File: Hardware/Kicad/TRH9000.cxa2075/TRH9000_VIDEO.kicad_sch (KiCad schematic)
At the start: 30 parts, among them J1 S-Video, J2 RGB, Q1 BC817, U6 CXA2075M

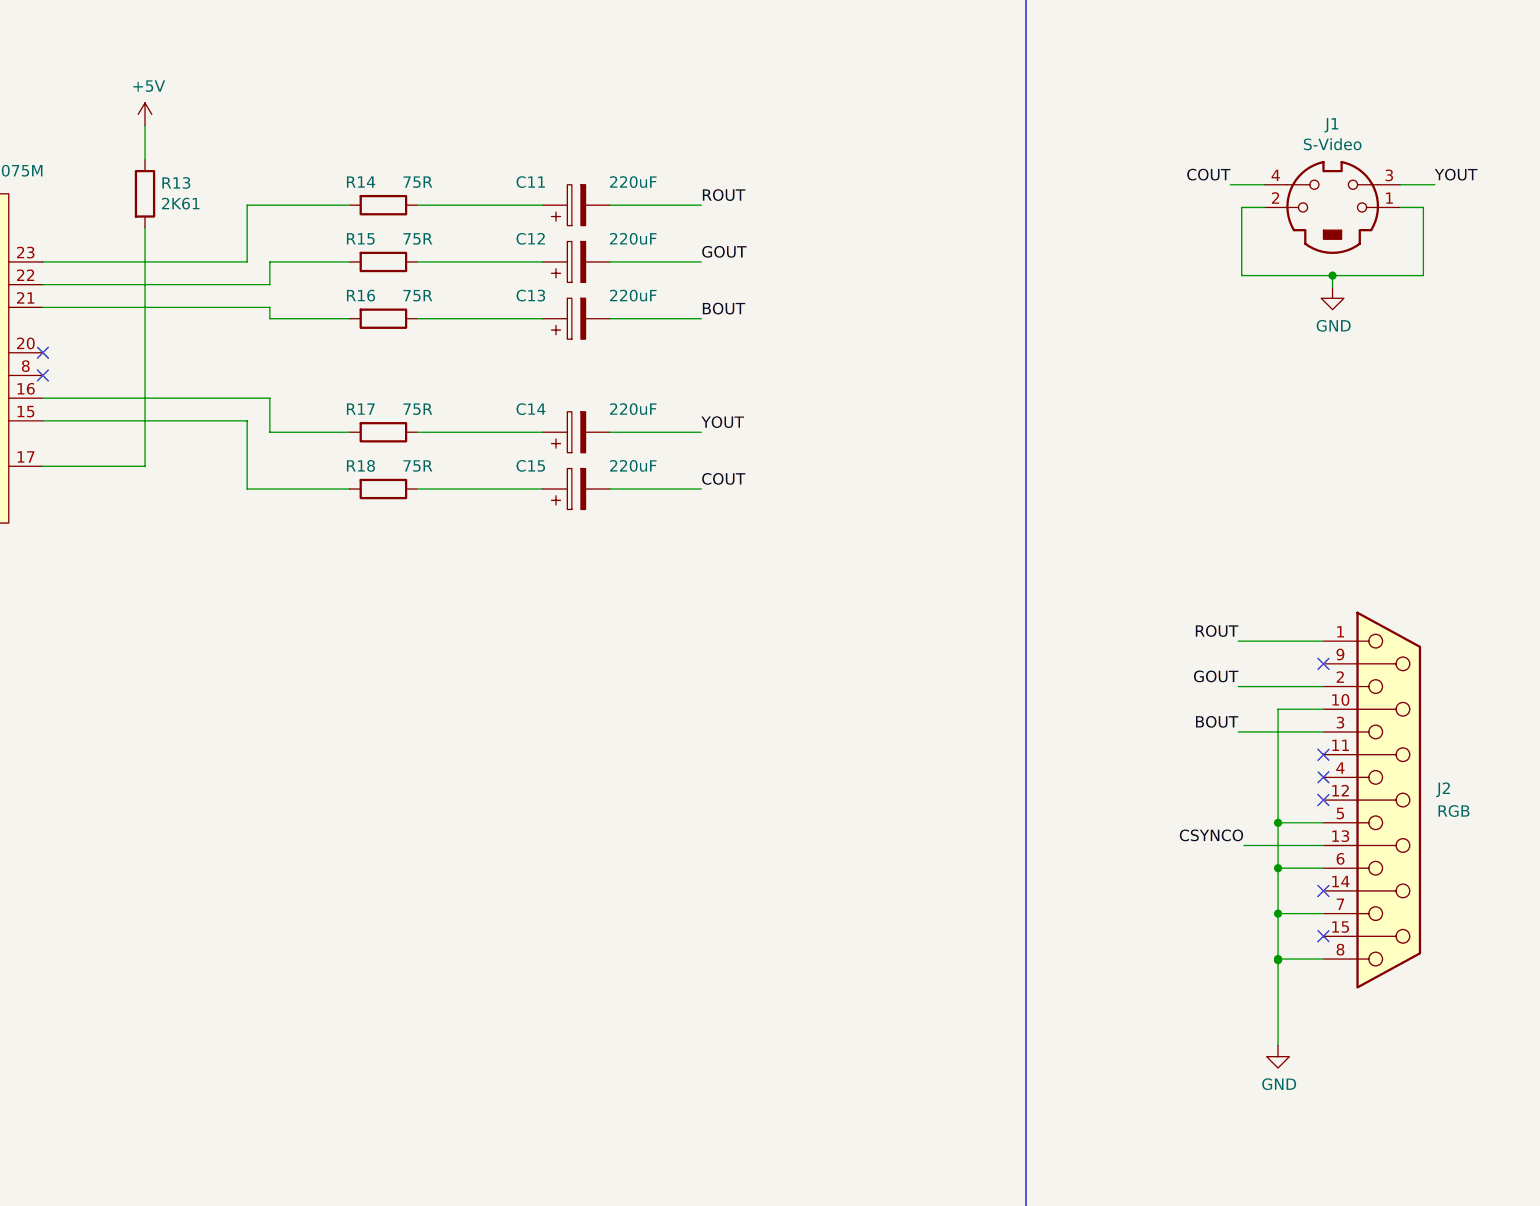
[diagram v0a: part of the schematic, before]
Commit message: small fix on the YTRAP to use internal for NTSC.
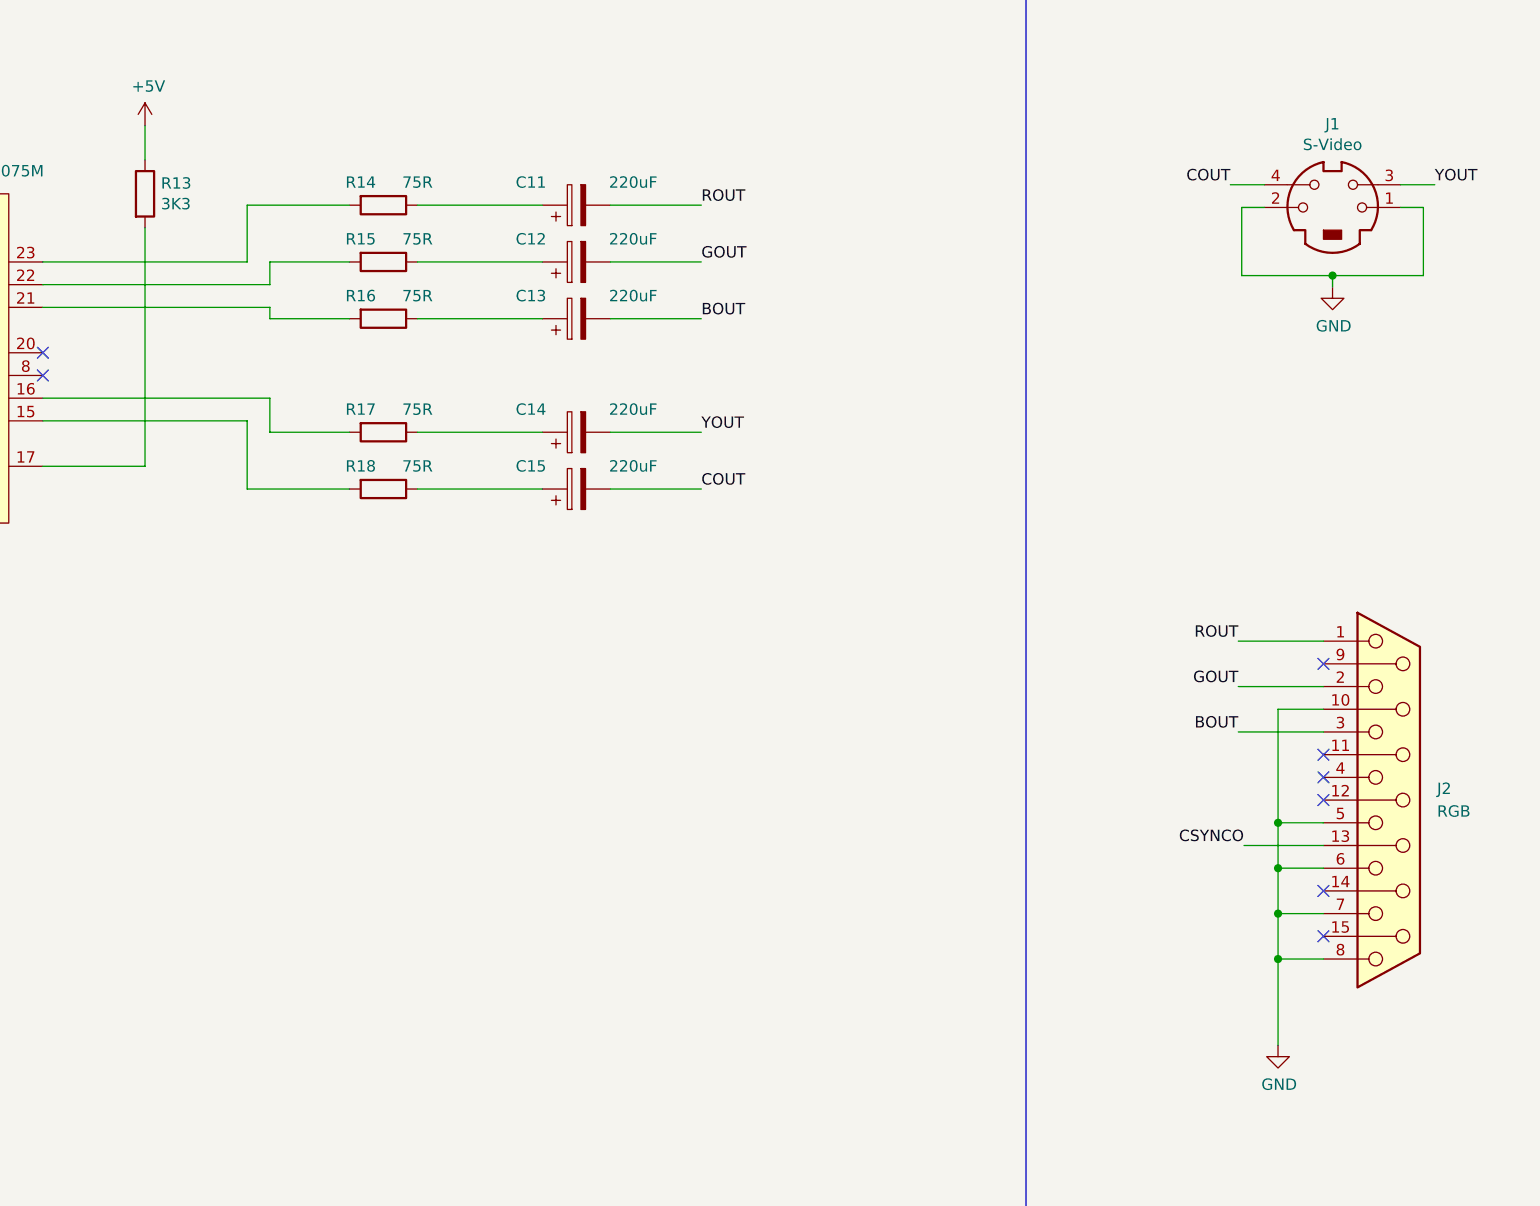
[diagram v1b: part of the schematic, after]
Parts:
- R13: value 2K61 -> 3K3

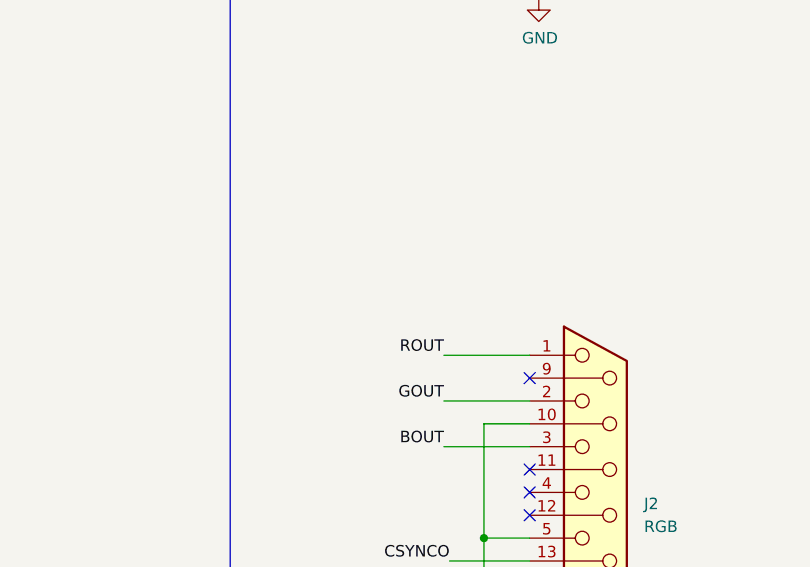
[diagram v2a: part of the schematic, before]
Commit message: Jumper to provide 5V to SCART cables
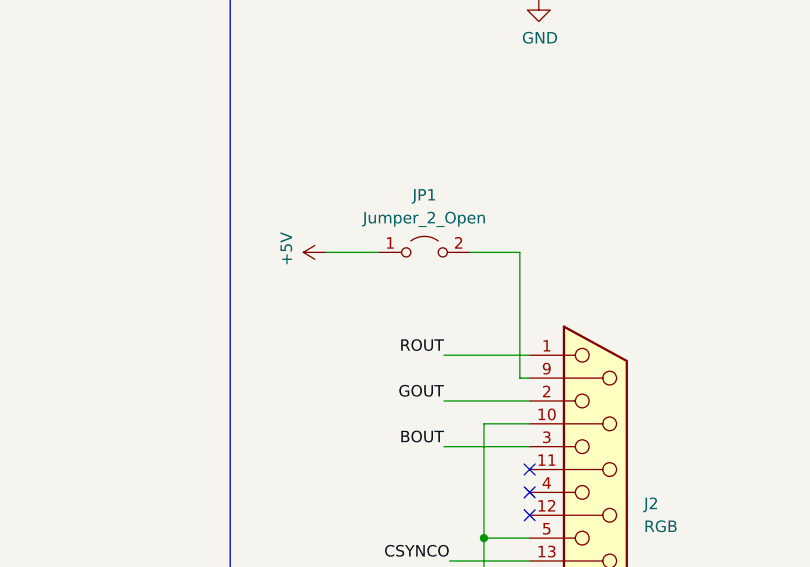
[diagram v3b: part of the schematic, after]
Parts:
- added JP1: Jumper_2_Open, Jumper:SolderJumper-2_P1.3mm_Open_Pad1.0x1.5mm, symbol Jumper:Jumper_2_Open
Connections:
- net +5V: now also JP1.1 (A)
- net at J2.9 (P9): now also JP1.2 (B)
- no-connect marks 8 -> 7
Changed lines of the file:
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@@
   (no_connect (at 165.608 113.284))
   (no_connect (at 308.864 170.942))
-  (no_connect (at 308.864 145.542))
   (no_connect (at 308.864 158.242))
   (no_connect (at 165.608 110.744))
@@
     (stroke (width 0) (type default))
   )
+  (wire (pts (xy 307.7718 145.542) (xy 307.7718 131.572))
+    (stroke (width 0) (type default))
+  )
   (wire (pts (xy 152.908 80.264) (xy 152.908 81.534))
     (stroke (width 0) (type default))
@@
     (stroke (width 0) (type default))
   )
+  (wire (pts (xy 302.26 131.572) (xy 307.7718 131.572))
+    (stroke (width 0) (type default))
+  )
   (wire (pts (xy 100.33 200.406) (xy 112.014 200.406))
     (stroke (width 0) (type default))
@@
     (stroke (width 0) (type default))
   )
+  (wire (pts (xy 308.864 145.542) (xy 307.7718 145.542))
+    (stroke (width 0) (type default))
+  )
   (wire (pts (xy 80.518 110.744) (xy 80.518 113.284))
     (stroke (width 0) (type default))
@@
   )
   (wire (pts (xy 165.608 103.124) (xy 191.008 103.124))
+    (stroke (width 0) (type default))
+  )
+  (wire (pts (xy 286.258 131.572) (xy 292.1 131.572))
     (stroke (width 0) (type default))
   )
@@
     )
   )
+  (symbol (lib_id "power:+5V") (at 286.258 131.572 90) (unit 1)
+    (in_bom yes) (on_board yes) (dnp no)
+    (property "Reference" "#PWR047" (at 290.068 131.572 0)
+      (effects (font (size 1.27 1.27)) hide)
+    )
+    (property "Value" "+5V" (at 281.8638 131.191 0)
+      (effects (font (size 1.27 1.27)))
+    )
+    (property "Footprint" "" (at 286.258 131.572 0)
+      (effects (font (size 1.27 1.27)) hide)
+    )
+    (property "Datasheet" "" (at 286.258 131.572 0)
+      (effects (font (size 1.27 1.27)) hide)
+    )
+    (pin "1")
+    (instances
+      (project "TRH9000"
+        (path "/1a0ec755-0979-4213-9180-0cd879831c1c/d9ed34ef-ff83-4a70-a9f7-db0f42d1292e"
+          (reference "#PWR047") (unit 1)
+        )
+      )
+    )
+  )
   (symbol (lib_id "Device:C") (at 80.518 117.094 0) (unit 1)
     (in_bom yes) (on_board yes) (dnp no)
@@
         )
       )
+    )
+  )
+  (symbol (lib_id "Jumper:Jumper_2_Open") (at 297.18 131.572 0) (unit 1)
+    (in_bom yes) (on_board yes) (dnp no) (fields_autoplaced)
+    (property "Reference" "JP1" (at 297.18 125.222 0)
+      (effects (font (size 1.27 1.27)))
+    )
+    (property "Value" "Jumper_2_Open" (at 297.18 127.762 0)
+      (effects (font (size 1.27 1.27)))
+    )
+    (property "Footprint" "Jumper:SolderJumper-2_P1.3mm_Open_Pad1.0x1.5mm" (at 297.18 131.572 0)
+      (effects (font (size 1.27 1.27)) hide)
+    )
+    (property "Datasheet" "~" (at 297.18 131.572 0)
+      (effects (font (size 1.27 1.27)) hide)
+    )
+    (pin "1")
+    (pin "2")
+    (instances
+      (project "TRH9000"
+        (path "/1a0ec755-0979-4213-9180-0cd879831c1c/d9ed34ef-ff83-4a70-a9f7-db0f42d1292e"
+          (reference "JP1") (unit 1)
+        )
+      )

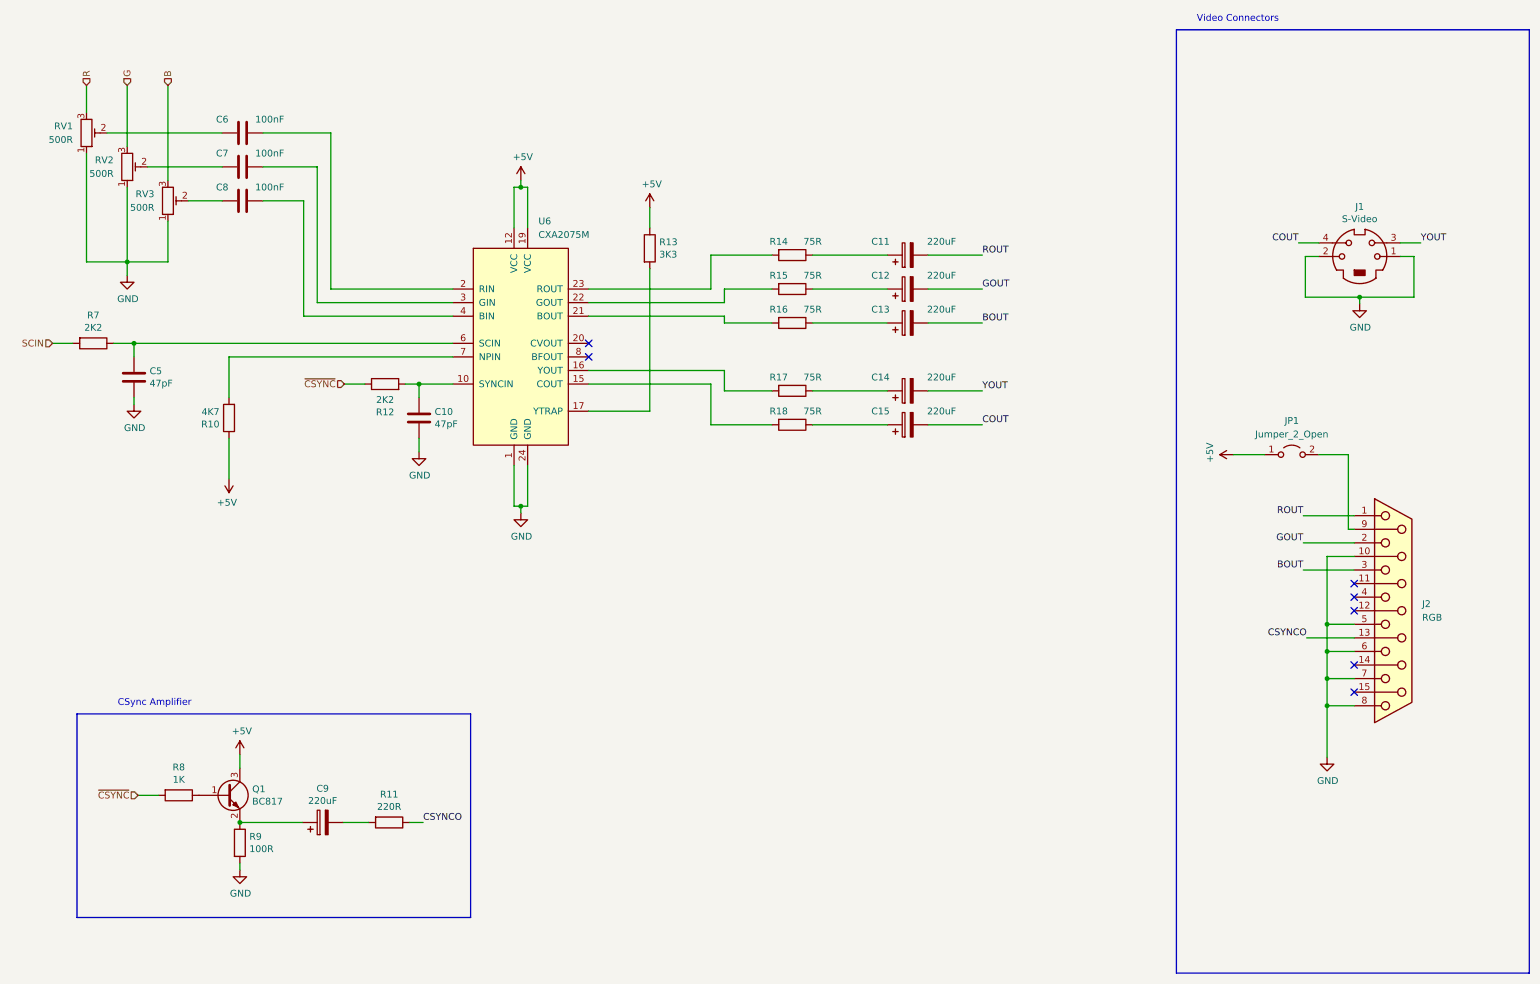
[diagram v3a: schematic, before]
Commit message: Exposing composite, footprint and silk corrections
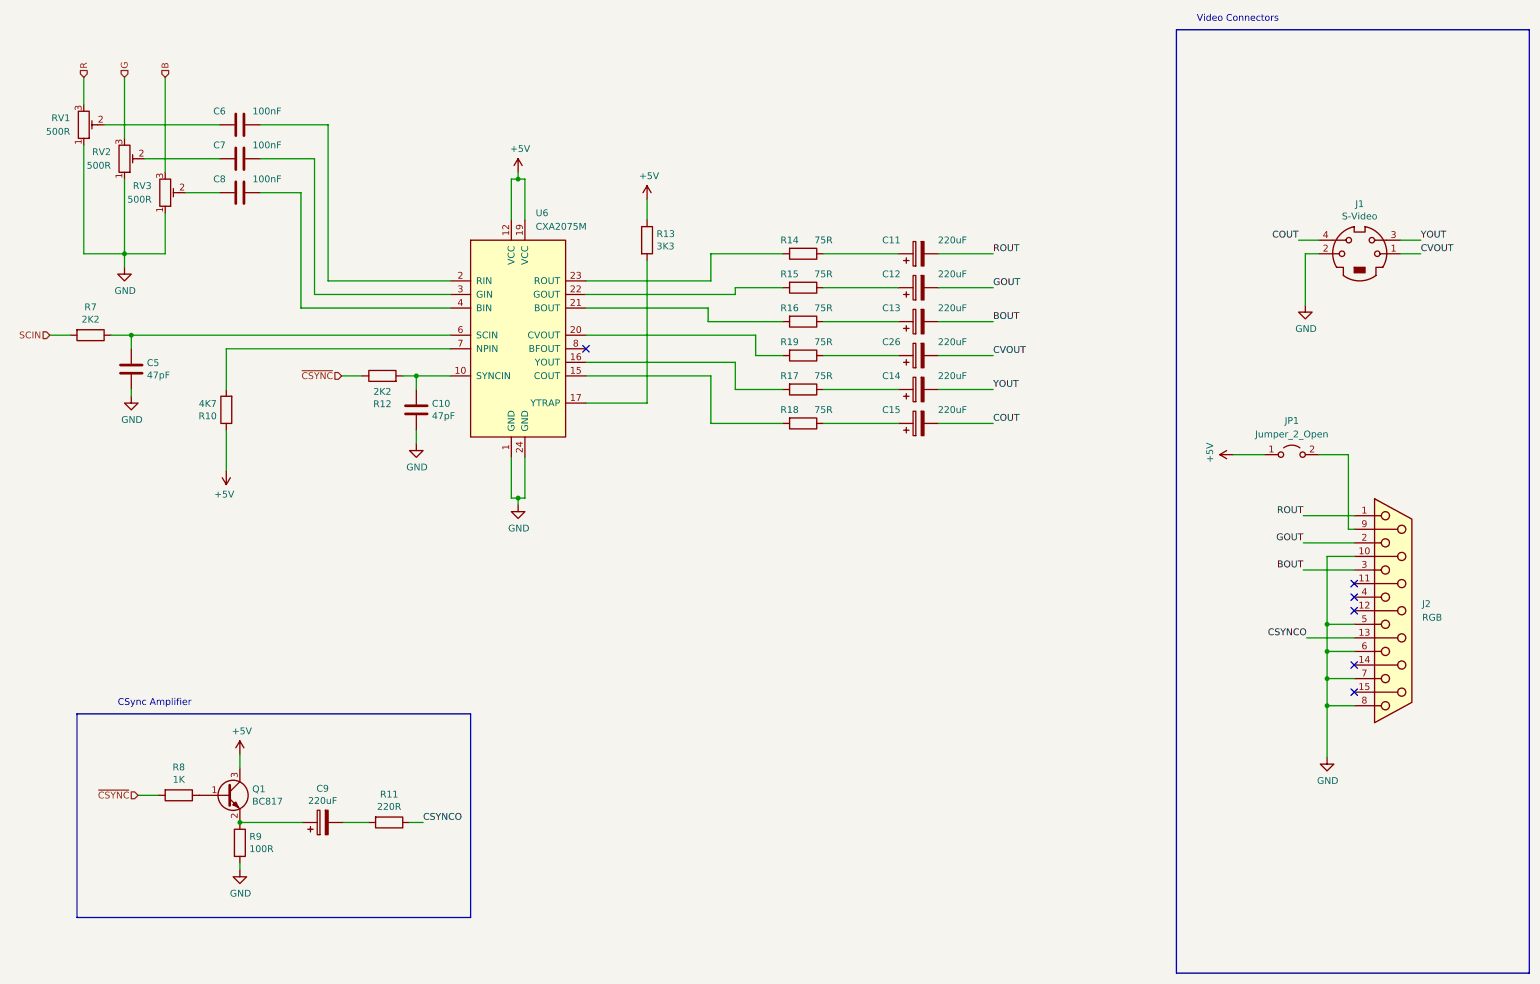
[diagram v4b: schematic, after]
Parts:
- added C26: 220uF, Capacitor_Tantalum_SMD:CP_EIA-3528-15_AVX-H, symbol Device:C_Polarized
- added R19: 75R, Resistor_SMD:R_0805_2012Metric, symbol Device:R
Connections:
- net GND: no longer J1.1
- net at U6.20 (CVOUT): now also R19.2
- new net: C26.1, R19.1
- new net CVOUT: C26.2, J1.1
- no-connect marks 7 -> 6
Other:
- moved on the sheet: C10, C11, C12, C13, C14, C15, C5, C6, C7, C8, J1, R10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

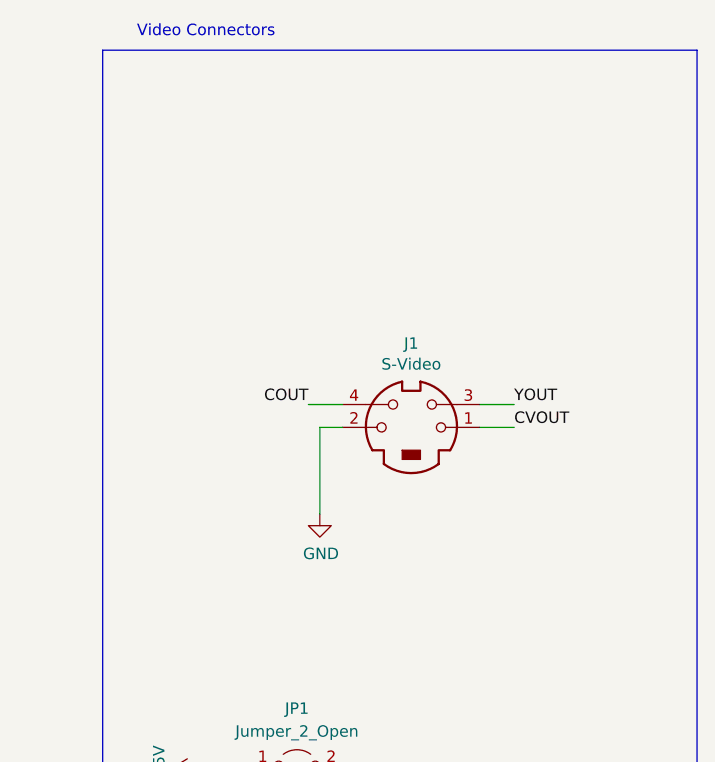
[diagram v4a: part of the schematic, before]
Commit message: Updates  to have Svideo and Composite exposed via appropriate connectors
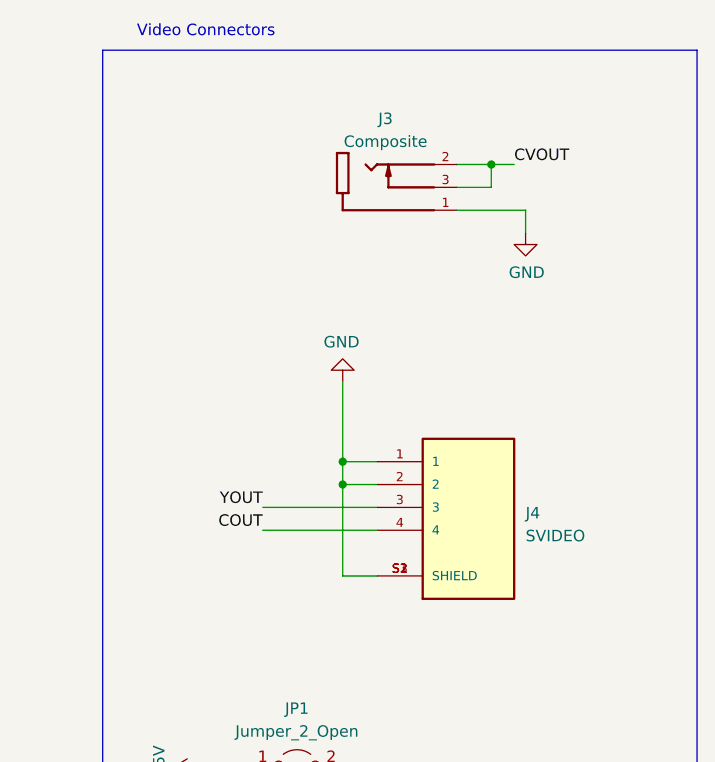
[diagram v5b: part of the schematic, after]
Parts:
- removed J1: S-Video, Connector_PinHeader_2.54mm:PinHeader_1x04_P2.54mm_Vertical, symbol Connector:Mini-DIN-4
- added J3: Composite, Footprints:SWITCHCRAFT_PJRAN1X1U02AUX, symbol PJRAN1X1U02AUX:PJRAN1X1U02AUX
- added J4: SVIDEO, Footprints:CUI_MD-40SM, symbol MD-40SM:MD-40SM
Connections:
- net COUT: now also J4.4
- net CVOUT: now also J3.2, J3.3
- net GND: now also J3.1, J4.1, J4.2, J4.S1 (SHIELD), J4.S2 (SHIELD), J4.S3 (SHIELD)
- net YOUT: now also J4.3
